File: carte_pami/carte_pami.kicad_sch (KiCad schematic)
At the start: 21 parts, among them J1 Conn_01x04_Pin, J2 Conn_01x04_Pin, J3 Conn_01x05_Pin, J4 Screw_Terminal_01x02, M1 Motor_Servo, M2 Motor_Servo, U1 NUCLEO32-L432KC, U2 R-78E5.0-1.0

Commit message: schematique pami
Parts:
- removed R1: R_Photo, symbol Device:R_Photo
- added C3, C4: 10uF, Capacitor_SMD:C_0805_2012Metric, symbol Device:C
- added J5, J6: Conn_01x02_Pin, Connector_PinHeader_2.54mm:PinHeader_1x02_P2.54mm_Vertical, symbol Connector:Conn_01x02_Pin
- added J7: Conn_01x05_Pin, Connector_PinHeader_2.54mm:PinHeader_1x05_P2.54mm_Vertical, symbol Connector:Conn_01x05_Pin
- added J8: Conn_01x04_Pin, Connector_PinHeader_2.54mm:PinHeader_1x04_P2.54mm_Vertical, symbol Connector:Conn_01x04_Pin
- added R1, R2: 500, Resistor_SMD:R_0805_2012Metric, symbol Device:R_Small
- added R3: R_Photo, Connector_PinHeader_2.54mm:PinHeader_1x02_P2.54mm_Vertical, symbol Device:R_Photo
- added R4: 10k, Resistor_SMD:R_0805_2012Metric, symbol Device:R_Small
- C1, C2: footprint (none) -> Capacitor_SMD:C_0805_2012Metric
- D1, D2: footprint (none) -> LED_SMD:LED_0603_1608Metric
- J3: footprint (none) -> Connector_PinHeader_2.54mm:PinHeader_1x05_P2.54mm_Vertical
- J4: footprint (none) -> TerminalBlock:TerminalBlock_bornier-2_P5.08mm
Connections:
- net +12V is gone; now on net ALIM: A1.8 (VMOT), A2.8 (VMOT), C1.1, C2.1
- net +3.3V: now also J7.1 (Pin_1), R3.1
- net +5V: now also D1.2 (A), U2.3 (OUT), J8.1 (Pin_1)
- net GND: now also J4.1 (Pin_1), U2.2 (GND), C3.1, C4.1, J5.2 (Pin_2), J6.2 (Pin_2), J7.2 (Pin_2), J8.2 (Pin_2), R1.2, R2.1, R4.1
- net SCL: now also J7.4 (Pin_4)
- net SDA: now also J7.3 (Pin_3)
- net at D2.1 (K): now also R1.1
- net LED: now reaches D2.2 (A)
- net LED: now also U1.16 (PB03)
- net ALIM: now reaches U2.1 (IN)
- net ALIM: now also J4.2 (Pin_2), C3.2, C4.2
- net TX: now reaches U1.1 (PA09)
- net TX: now also J8.3 (Pin_3)
- net SHUTDOWN1: now reaches U1.19 (PA00)
- net SHUTDOWN1: now also J3.5 (Pin_5)
- net RX: now reaches U1.2 (PA10)
- net RX: now also J8.4 (Pin_4)
- net FDC2: now reaches U1.22 (PA04)
- net FDC2: now also J6.1 (Pin_1)
- net FDC1: now reaches U1.23 (PA05)
- net FDC1: now also J5.1 (Pin_1)
- net SHUTDOWN2: now reaches U1.24 (PA06)
- net SHUTDOWN2: now also J7.5 (Pin_5)
- net at D1.1 (K): now also R2.2
- net PHTORES_ADC renamed MEAS_LIGHT
- net MEAS_LIGHT: now also R3.2, R4.2
- no-connect marks 6 -> 9
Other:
- note removed: "Alimenter une led directement par le 5V, et une led connectée à une broche de la nucleo (PB03)."
- note removed: "Faire un pont diviseur de tension, avec une résistance de 10k et la photorésistance."
- note removed: "Fin de courses ! (un connecteur avec une pin à la masse, et une pin connectée à la nucleo)"
- note removed: "mettre 2 connecteurs, avec SDA et SCL en //, et chaque dernière broche connectée (indépendement) à la nucleo"
- moved on the sheet: J4, U2

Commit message: placement composantes
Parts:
- added H1, H2, H3, H4: MountingHole, MountingHole:MountingHole_3.2mm_M3, symbol Mechanical:MountingHole
- C1, C2: footprint Capacitor_SMD:C_0805_2012Metric -> Capacitor_SMD:CP_Elec_10x12.5
- J1, J2: value Conn_01x04_Pin -> STEPPER
- J3, J7: value Conn_01x05_Pin -> RANGE
- J5: value Conn_01x02_Pin -> FDC2
- J6: value Conn_01x02_Pin -> FDC1
- J8: value Conn_01x04_Pin -> UART
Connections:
- net SHUTDOWN1: now also U1.9 (PB01); no longer U1.19 (PA00)
- net SHUTDOWN2: now also U1.6 (PB00); no longer U1.24 (PA06)
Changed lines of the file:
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@@
   (no_connect (at 154.94 102.87))
   (no_connect (at 132.08 95.25))
-  (no_connect (at 132.08 92.71))
   (no_connect (at 154.94 77.47))
   (no_connect (at 154.94 72.39))
   (no_connect (at 132.08 77.47))
-  (no_connect (at 132.08 85.09))
+  (no_connect (at 154.94 100.33))
+  (no_connect (at 154.94 87.63))
   (no_connect (at 132.08 97.79))
   (wire (pts (xy 215.9 63.5) (xy 215.9 66.04))
@@
     (stroke (width 0) (type default))
   )
-  (global_label "SHUTDOWN2" (shape input) (at 154.94 87.63 0) (fields_autoplaced)
-    (effects (font (size 1.27 1.27)) (justify left))
-    (property "Intersheetrefs" "${INTERSHEET_REFS}" (at 169.3552 87.63 0)
-      (effects (font (size 1.27 1.27)) (justify left) hide)
+  (global_label "SHUTDOWN2" (shape input) (at 132.08 85.09 180) (fields_autoplaced)
+    (effects (font (size 1.27 1.27)) (justify right))
+    (property "Intersheetrefs" "${INTERSHEET_REFS}" (at 117.6648 85.09 0)
+      (effects (font (size 1.27 1.27)) (justify right) hide)
     )
   )
@@
     )
   )
-  (global_label "SHUTDOWN1" (shape input) (at 154.94 100.33 0) (fields_autoplaced)
-    (effects (font (size 1.27 1.27)) (justify left))
-    (property "Intersheetrefs" "${INTERSHEET_REFS}" (at 169.3552 100.33 0)
-      (effects (font (size 1.27 1.27)) (justify left) hide)
+  (global_label "SHUTDOWN1" (shape input) (at 132.08 92.71 180) (fields_autoplaced)
+    (effects (font (size 1.27 1.27)) (justify right))
+    (property "Intersheetrefs" "${INTERSHEET_REFS}" (at 117.6648 92.71 0)
+      (effects (font (size 1.27 1.27)) (justify right) hide)
     )
   )
@@
       (effects (font (size 1.27 1.27)))
     )
-    (property "Value" "Conn_01x04_Pin" (at 107.315 38.1 0)
+    (property "Value" "UART" (at 107.315 38.1 0)
       (effects (font (size 1.27 1.27)))
     )
@@
       (effects (font (size 1.27 1.27)))
     )
-    (property "Value" "Conn_01x02_Pin" (at 168.275 158.75 0)
+    (property "Value" "FDC2" (at 168.275 158.75 0)
       (effects (font (size 1.27 1.27)))
     )
@@
       (effects (font (size 1.27 1.27)))
     )
-    (property "Value" "Conn_01x02_Pin" (at 133.985 158.75 0)
+    (property "Value" "FDC1" (at 133.985 158.75 0)
       (effects (font (size 1.27 1.27)))
     )
@@
       (effects (font (size 1.27 1.27)))
     )
-    (property "Footprint" "Capacitor_SMD:C_0805_2012Metric" (at 255.27 87.9348 0)
+    (property "Footprint" "Capacitor_SMD:CP_Elec_10x12.5" (at 255.27 87.9348 0)
       (effects (font (size 1.27 1.27)) hide)
     )
@@
       (effects (font (size 1.27 1.27)) (justify right))
     )
-    (property "Value" "Conn_01x04_Pin" (at 264.16 111.76 0)
+    (property "Value" "STEPPER" (at 264.16 111.76 0)
       (effects (font (size 1.27 1.27)) (justify right))
     )
@@
         (path "/770e3594-3810-453e-8716-93c8c49f73f3"
           (reference "#PWR013") (unit 1)
+        )
+      )
+    )
+  )
+  (symbol (lib_id "Mechanical:MountingHole") (at 83.82 186.69 0) (unit 1)
+    (in_bom yes) (on_board yes) (dnp no) (fields_autoplaced)
+    (property "Reference" "H3" (at 86.36 185.42 0)
+      (effects (font (size 1.27 1.27)) (justify left))
+    )
+    (property "Value" "MountingHole" (at 86.36 187.96 0)
+      (effects (font (size 1.27 1.27)) (justify left))
+    )
+    (property "Footprint" "MountingHole:MountingHole_3.2mm_M3" (at 83.82 186.69 0)
+      (effects (font (size 1.27 1.27)) hide)
+    )
+    (property "Datasheet" "~" (at 83.82 186.69 0)
+      (effects (font (size 1.27 1.27)) hide)
+    )
+    (instances
+      (project "carte_pami"
+        (path "/770e3594-3810-453e-8716-93c8c49f73f3"
+          (reference "H3") (unit 1)
         )
       )
@@
       (effects (font (size 1.27 1.27)) (justify right))
     )
-    (property "Value" "Conn_01x04_Pin" (at 264.16 53.34 0)
+    (property "Value" "STEPPER" (at 264.16 53.34 0)
       (effects (font (size 1.27 1.27)) (justify right))
     )
@@
       (effects (font (size 1.27 1.27)))
     )
-    (property "Value" "Conn_01x05_Pin" (at 159.385 35.56 0)
+    (property "Value" "RANGE" (at 159.385 35.56 0)
       (effects (font (size 1.27 1.27)))
     )
@@
     )
   )
+  (symbol (lib_id "Mechanical:MountingHole") (at 83.82 191.77 0) (unit 1)
+    (in_bom yes) (on_board yes) (dnp no) (fields_autoplaced)
+    (property "Reference" "H4" (at 86.36 190.5 0)
+      (effects (font (size 1.27 1.27)) (justify left))
+    )
+    (property "Value" "MountingHole" (at 86.36 193.04 0)
+      (effects (font (size 1.27 1.27)) (justify left))
+    )
+    (property "Footprint" "MountingHole:MountingHole_3.2mm_M3" (at 83.82 191.77 0)
+      (effects (font (size 1.27 1.27)) hide)
+    )
+    (property "Datasheet" "~" (at 83.82 191.77 0)
+      (effects (font (size 1.27 1.27)) hide)
+    )
+    (instances
+      (project "carte_pami"
+        (path "/770e3594-3810-453e-8716-93c8c49f73f3"
+          (reference "H4") (unit 1)
+        )
+      )
+    )
+  )
+  (symbol (lib_id "Mechanical:MountingHole") (at 83.82 181.61 0) (unit 1)
+    (in_bom yes) (on_board yes) (dnp no) (fields_autoplaced)
+    (property "Reference" "H2" (at 86.36 180.34 0)
+      (effects (font (size 1.27 1.27)) (justify left))
+    )
+    (property "Value" "MountingHole" (at 86.36 182.88 0)
+      (effects (font (size 1.27 1.27)) (justify left))
+    )
+    (property "Footprint" "MountingHole:MountingHole_3.2mm_M3" (at 83.82 181.61 0)
+      (effects (font (size 1.27 1.27)) hide)
+    )
+    (property "Datasheet" "~" (at 83.82 181.61 0)
+      (effects (font (size 1.27 1.27)) hide)
+    )
+    (instances
+      (project "carte_pami"
+        (path "/770e3594-3810-453e-8716-93c8c49f73f3"
+          (reference "H2") (unit 1)
+        )
+      )
+    )
+  )
   (symbol (lib_id "power:GND") (at 177.8 163.83 90) (unit 1)
     (in_bom yes) (on_board yes) (dnp no) (fields_autoplaced)
@@
     )
   )
+  (symbol (lib_id "Mechanical:MountingHole") (at 83.82 176.53 0) (unit 1)
+    (in_bom yes) (on_board yes) (dnp no) (fields_autoplaced)
+    (property "Reference" "H1" (at 86.36 175.26 0)
+      (effects (font (size 1.27 1.27)) (justify left))
+    )
+    (property "Value" "MountingHole" (at 86.36 177.8 0)
+      (effects (font (size 1.27 1.27)) (justify left))
+    )
+    (property "Footprint" "MountingHole:MountingHole_3.2mm_M3" (at 83.82 176.53 0)
+      (effects (font (size 1.27 1.27)) hide)
+    )
+    (property "Datasheet" "~" (at 83.82 176.53 0)
+      (effects (font (size 1.27 1.27)) hide)
+    )
+    (instances
+      (project "carte_pami"
+        (path "/770e3594-3810-453e-8716-93c8c49f73f3"
+          (reference "H1") (unit 1)
+        )
+      )
+    )
+  )
   (symbol (lib_id "power:GND") (at 46.99 106.68 270) (unit 1)
     (in_bom yes) (on_board yes) (dnp no) (fields_autoplaced)
@@
       (effects (font (size 1.27 1.27)))
     )
-    (property "Footprint" "Capacitor_SMD:C_0805_2012Metric" (at 255.27 29.5148 0)
+    (property "Footprint" "Capacitor_SMD:CP_Elec_10x12.5" (at 255.27 29.5148 0)
       (effects (font (size 1.27 1.27)) hide)
     )
@@
       (effects (font (size 1.27 1.27)))
     )
-    (property "Value" "Conn_01x05_Pin" (at 133.985 36.83 0)
-      (effects (font (size 1.27 1.27)))
-    )
+    (property "Value" "RANGE" (at 133.985 36.83 0)
+      (effects (font (size 1.27 1.27)))
+    )

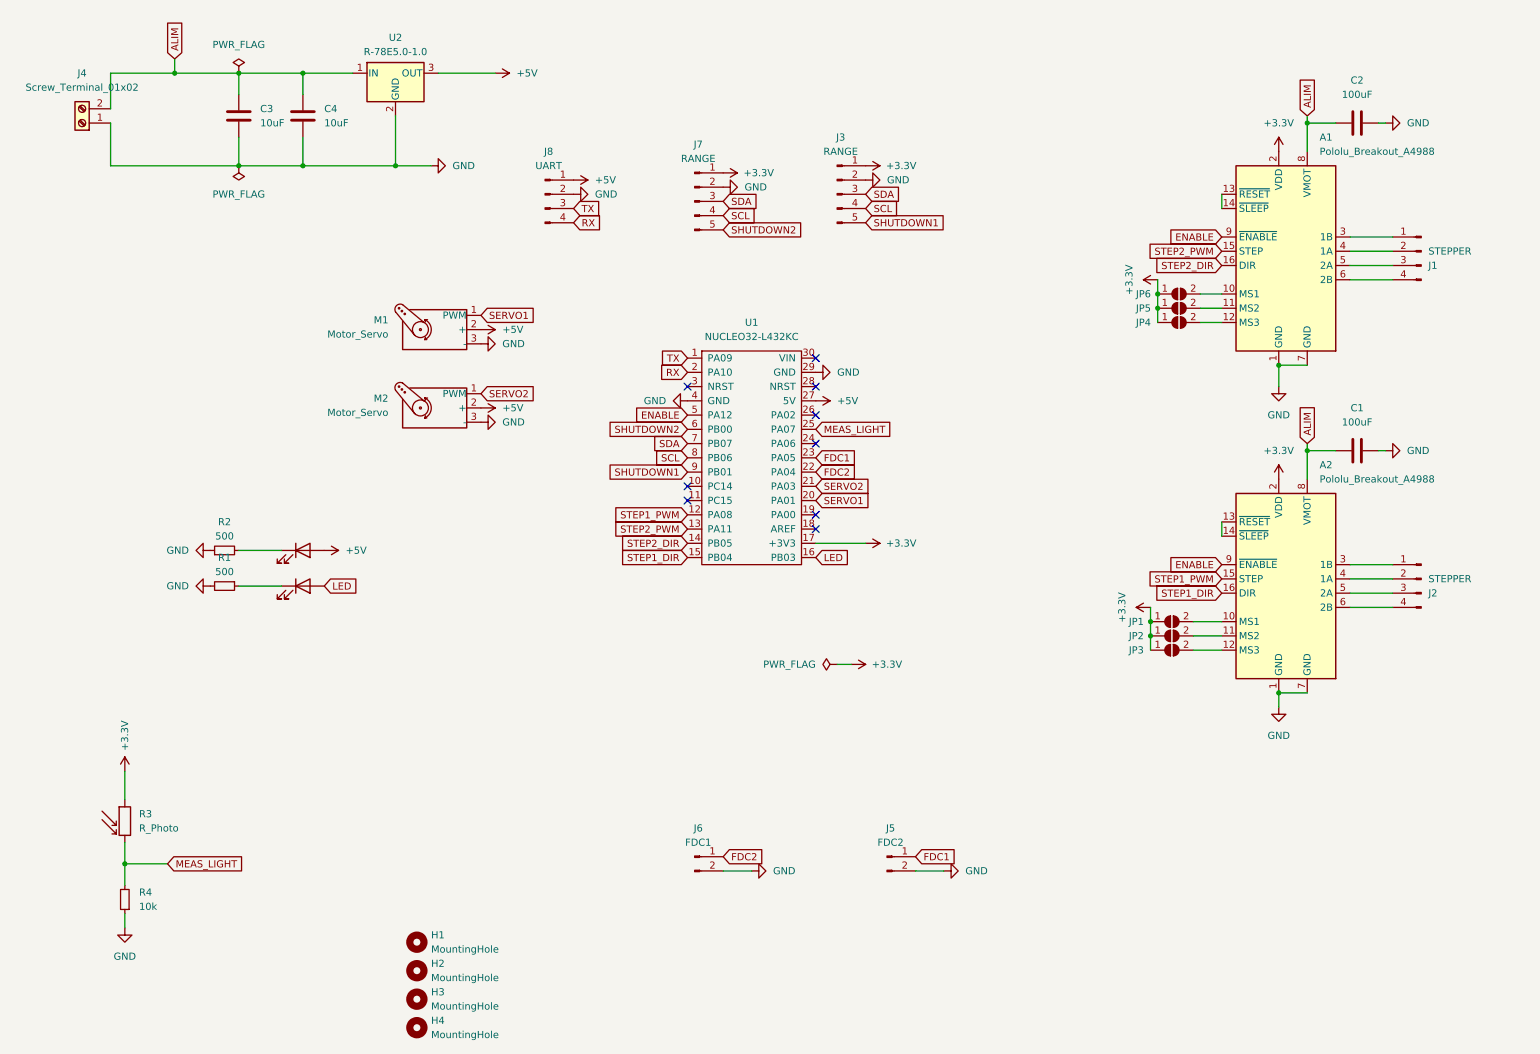
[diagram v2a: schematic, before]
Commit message: Petits ajouts au schéma, et définition des capabilities.
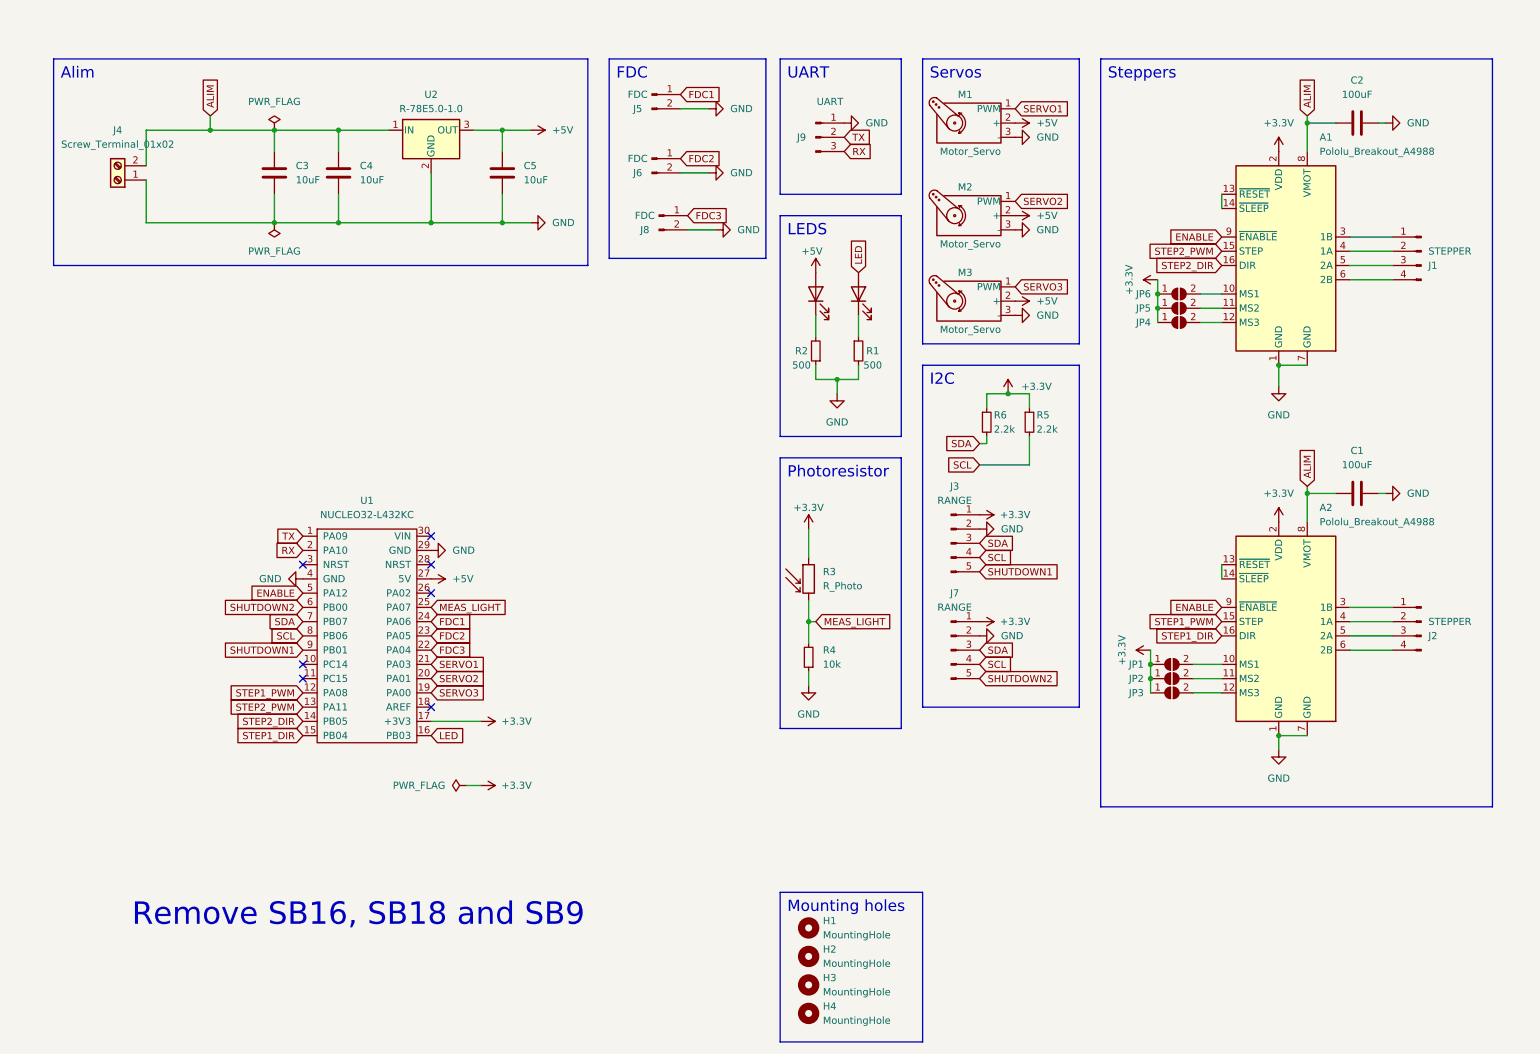
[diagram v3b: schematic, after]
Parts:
- removed J8: UART, Connector_PinHeader_2.54mm:PinHeader_1x04_P2.54mm_Vertical, symbol Connector:Conn_01x04_Pin
- added C5: 10uF, Capacitor_SMD:C_0805_2012Metric, symbol Device:C
- added J8: FDC, Connector_PinHeader_2.54mm:PinHeader_1x02_P2.54mm_Vertical, symbol Connector:Conn_01x02_Pin
- added J9: UART, Connector_PinHeader_2.54mm:PinHeader_1x03_P2.54mm_Vertical, symbol Connector:Conn_01x03_Pin
- added M3: Motor_Servo, Connector_PinHeader_2.54mm:PinHeader_1x03_P2.54mm_Vertical, symbol Motor:Motor_Servo
- added R5, R6: 2.2k, Resistor_SMD:R_0805_2012Metric, symbol Device:R_Small
- J5: value FDC2 -> FDC
- J6: value FDC1 -> FDC
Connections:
- net +3.3V: now also R5.1, R6.1
- net +5V: now also C5.2, M3.2 (+)
- net FDC1: now also U1.24 (PA06); no longer U1.23 (PA05)
- net FDC2: now also U1.23 (PA05); no longer U1.22 (PA04)
- net GND: now also C5.1, J8.2 (Pin_2), J9.1 (Pin_1), M3.3 (-)
- net RX: now also J9.3 (Pin_3)
- net SCL: now also R5.2
- net SDA: now also R6.2
- net SERVO1: now also U1.21 (PA03); no longer U1.20 (PA01)
- net SERVO2: now also U1.20 (PA01); no longer U1.21 (PA03)
- net TX: now also J9.2 (Pin_2)
- net SERVO3: now reaches U1.19 (PA00)
- net SERVO3: now also M3.1 (PWM)
- new net FDC3: J8.1 (Pin_1), U1.22 (PA04)
- no-connect marks 9 -> 7
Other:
- note added: "Alim"
- note added: "FDC"
- note added: "I2C"
- note added: "LEDS"
- note added: "Mounting holes"
- note added: "Photoresistor"
- note added: "Remove SB16, SB18 and SB9"
- note added: "Servos"
- note added: "Steppers"
- note added: "UART"
- moved on the sheet: A2, C1, C3, C4, H1, H2, H3, H4, J2, J3, J4, J5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
